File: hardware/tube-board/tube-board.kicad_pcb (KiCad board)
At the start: 2 copper layers, 182 x 26 mm, 18 parts, among them J1 CONN_01X10, J2 CONN_01X10, U1 HV5522PG, U2 HV5522PG

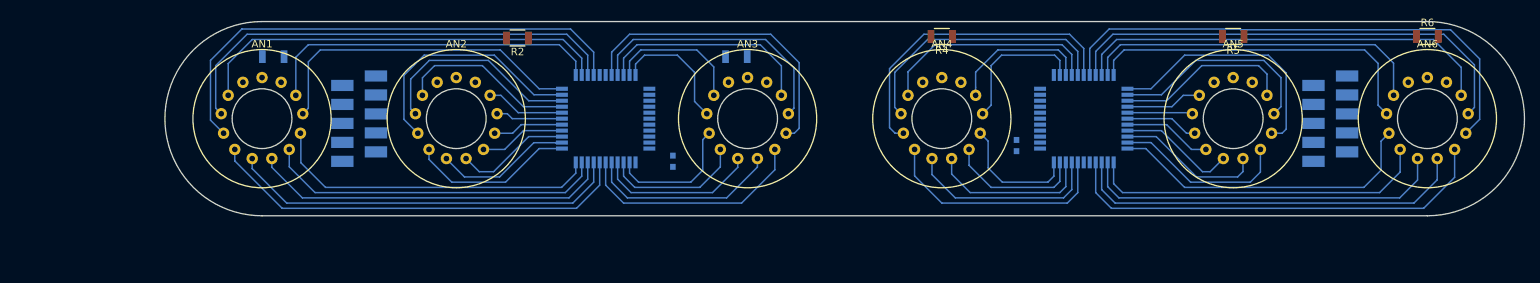
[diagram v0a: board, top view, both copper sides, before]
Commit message: Working on tube board layout
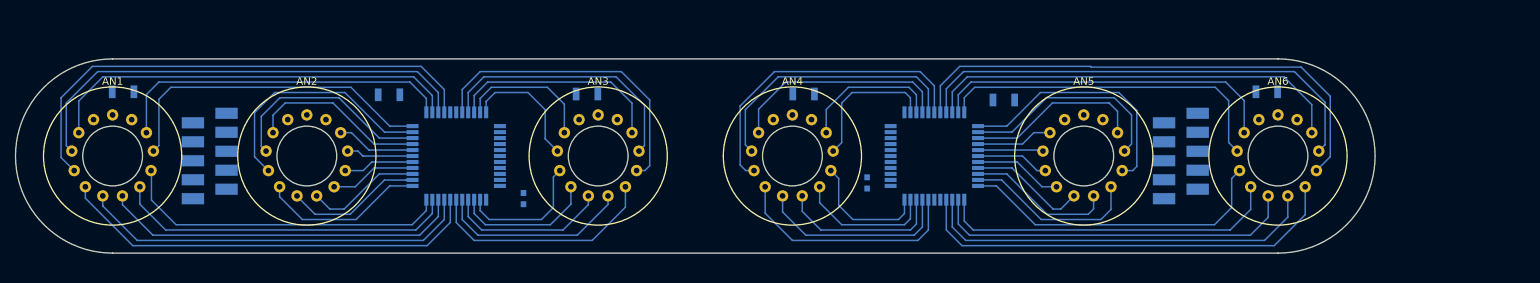
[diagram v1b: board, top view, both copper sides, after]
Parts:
- R2, R4, R5, R6: moved to B.Cu
- moved R5 31.9 mm to (181.3, 97.5), turned to 0 degrees
- moved R6 22.7 mm to (216.5, 96.4)
- moved R1 20.6 mm to (63.4, 96.4)
- moved AN1 20.6 mm to (62.0, 105.0)
- moved AN2 20.6 mm to (88.0, 105.0)
- moved AN3 20.6 mm to (127.0, 105.0)
- moved AN4 20.6 mm to (153.0, 105.0)
- moved AN5 20.6 mm to (192.0, 105.0)
- moved AN6 20.6 mm to (218.0, 105.0)
- moved C1 20.6 mm to (117.0, 110.7)
- moved C2 20.6 mm to (163.0, 108.6)
- moved J1 20.6 mm to (75.0, 105.0)
- moved J2 20.6 mm to (205.0, 105.0)
- moved R3 20.6 mm to (125.5, 96.7)
- moved U1 20.6 mm to (108.0, 105.0)
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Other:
- net class Default: trace_width 0.25 -> 0.2; via_dia 0.6 -> 0.5; via_drill 0.4 -> 0.34
- rule pad_to_mask_clearance: 0.2 -> 0.05

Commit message: Working on tube board layout
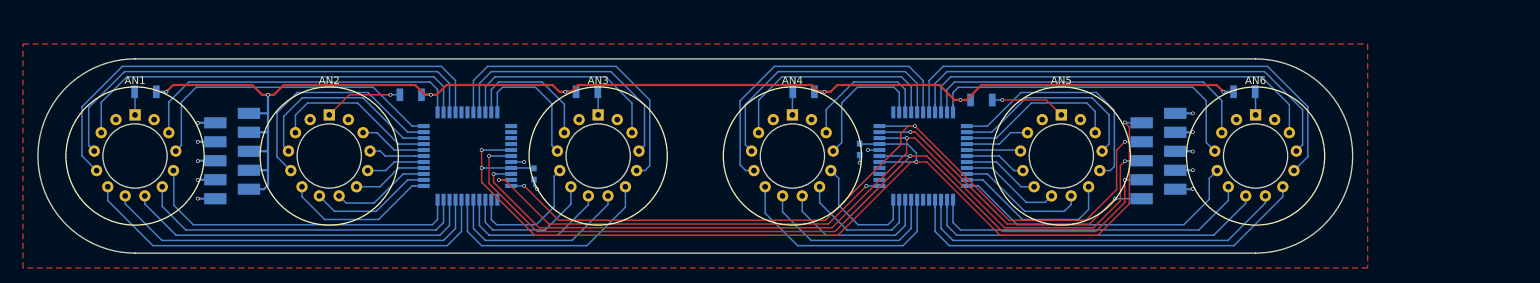
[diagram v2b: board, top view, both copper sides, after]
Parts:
- moved C2 4.61 mm to (162.0, 104.1), turned to 270 degrees
- moved C1 3.58 mm to (118.4, 107.4)
- moved R1 3.00 mm to (66.4, 96.4)
- moved AN1 3.00 mm to (65.0, 105.0)
- moved AN2 3.00 mm to (91.0, 105.0)
- moved AN5 3.00 mm to (189.0, 105.0)
- moved AN6 3.00 mm to (215.0, 105.0)
- moved J1 3.00 mm to (78.0, 105.0)
- moved J2 3.00 mm to (202.0, 105.0)
- moved R5 3.00 mm to (178.3, 97.5)
- moved R6 3.00 mm to (213.5, 96.4)
- moved R2 2.90 mm to (101.9, 96.8)
- moved U1 1.50 mm to (109.5, 105.0)
- moved U2 1.50 mm to (170.5, 105.0)
- moved R3 0.30 mm to (125.5, 96.4)
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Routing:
- net HT: track 0.00 -> 180.8 mm, vias 0 -> 7
- net +12V: track 0.00 -> 142.5 mm, vias 0 -> 4
- net /LE: track 0.00 -> 114.0 mm, vias 0 -> 3
- net /CLK: track 0.00 -> 113.8 mm, vias 0 -> 3
- net /BL: track 0.00 -> 109.8 mm, vias 0 -> 3
- net Net-(U1-Pad32): track 0.00 -> 57.2 mm, vias 0 -> 2
- net /DATA_IN: track 0.00 -> 41.6 mm, vias 0 -> 2
- net GND: track 0.00 -> 29.4 mm, vias 0 -> 14
- net Net-(AN2-Pad1): track 0.00 -> 10.6 mm, vias 0 -> 1
- net Net-(AN5-Pad1): track 0.00 -> 10.1 mm, vias 0 -> 1
- net Net-(AN6-Pad1): track 0.00 -> 3.12 mm
- net Net-(AN4-Pad1): track 0.00 -> 3.12 mm
- net Net-(AN3-Pad1): track 0.00 -> 3.12 mm
- net Net-(AN1-Pad1): track 0.00 -> 3.12 mm
- net /HV57: track 58.4 -> 55.6 mm
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- added copper zone on F.Cu, net GND
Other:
- board size 182 x 26 mm -> 176 x 26 mm

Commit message: Working on tube board layout
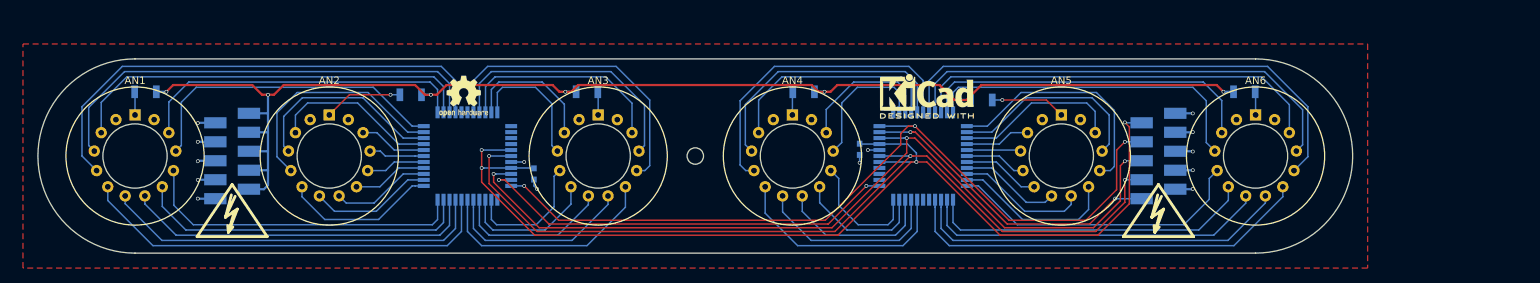
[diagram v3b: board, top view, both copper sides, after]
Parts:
- added REF**: Symbol_HighVoltage_Type2_CopperTop_VerySmall, radio-clock:Symbol_HighVoltage_Type2_SilkscreenTop_VerySmall, F.Cu at (202.0, 113.0)
- added REF**: MountingHole_2.2mm_M2, Mounting_Holes:MountingHole_2.2mm_M2, B.Cu at (140.0, 105.0)
- added REF**: Symbol_HighVoltage_Type2_CopperTop_VerySmall, radio-clock:Symbol_HighVoltage_Type2_SilkscreenTop_VerySmall, F.Cu at (78.0, 113.0)
- added REF***: OSHW-Logo2_7.3x6mm_SilkScreen, Symbols:OSHW-Logo2_7.3x6mm_SilkScreen, F.Cu at (109.0, 97.0)
- added REF***: KiCad-Logo2_6mm_SilkScreen, Symbols:KiCad-Logo2_6mm_SilkScreen, F.Cu at (171.0, 97.0)

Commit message: Working on main board schematic
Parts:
- removed the REF** at (202.0, 113.0)
- moved REF*** 62.8 mm to (170.0, 112.0)
- moved REF** 31.1 mm to (109.0, 111.0)
- moved REF*** 1.00 mm to (171.0, 98.0)
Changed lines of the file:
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@@
     (links 103)
     (no_connects 0)
-    (area 51.924999 91.924999 228.075001 118.075001)
+    (area 50 90 230.000001 120.000001)
     (thickness 1.6)
     (drawings 10)
     (tracks 540)
     (zones 0)
-    (modules 23)
+    (modules 22)
     (nets 100)
   )
@@
     (add_net /HV9)
   )
-  (module radio-clock:Symbol_HighVoltage_Type2_SilkscreenTop_VerySmall (layer F.Cu)
-    (at 202 113)
-    (descr "Symbol, High Voltage, Type 2, Copper Top, Very Small,")
-    (tags "Symbol, High Voltage, Type 2, Copper Top, Very Small,")
-    (fp_text reference REF** (at -0.127 -5.715) (layer F.SilkS) hide
-      (effects (font (size 1 1) (thickness 0.15)))
-    )
-    (fp_text value Symbol_HighVoltage_Type2_CopperTop_VerySmall (at -0.381 4.572) (layer F.Fab)
-      (effects (font (size 1 1) (thickness 0.15)))
-    )
-    (fp_line (start -0.49784 2.19964) (end 0.70104 -0.89916) (layer F.SilkS) (width 0.381))
-    (fp_line (start 0.70104 -0.89916) (end 0.1016 -0.50038) (layer F.SilkS) (width 0.381))
-    (fp_line (start -0.89916 0.20066) (end 0.40132 -2.60096) (layer F.SilkS) (width 0.381))
-    (fp_line (start -0.49784 2.19964) (end 0.1016 1.50114) (layer F.SilkS) (width 0.381))
-    (fp_line (start -0.09906 -2.79908) (end -0.89916 0.20066) (layer F.SilkS) (width 0.381))
-    (fp_line (start -0.89916 0.20066) (end 0.29972 -0.59944) (layer F.SilkS) (width 0.381))
-    (fp_line (start 0.29972 -0.59944) (end -0.49784 2.19964) (layer F.SilkS) (width 0.381))
-    (fp_line (start -0.49784 2.19964) (end -0.59944 1.30048) (layer F.SilkS) (width 0.381))
-    (fp_line (start 0 -4.191) (end 4.699 2.794) (layer F.SilkS) (width 0.381))
-    (fp_line (start 4.699 2.794) (end -4.699 2.794) (layer F.SilkS) (width 0.381))
-    (fp_line (start -4.699 2.794) (end 0 -4.191) (layer F.SilkS) (width 0.381))
-  )
   (module Capacitors_SMD:C_0603 (layer B.Cu)
     (at 118.4 107.4 270)
@@
   )
   (module Symbols:OSHW-Logo2_7.3x6mm_SilkScreen (layer F.Cu)
-    (at 109 97)
+    (at 170 112)
     (descr "Open Source Hardware Symbol")
     (tags "Logo Symbol OSHW")
@@
   )
   (module Symbols:KiCad-Logo2_6mm_SilkScreen (layer F.Cu)
-    (at 171 97)
+    (at 171 98)
     (descr "KiCad Logo")
     (tags "Logo KiCad")
@@
   )
   (module radio-clock:Symbol_HighVoltage_Type2_SilkscreenTop_VerySmall (layer F.Cu)
-    (at 78 113)
+    (at 109 111)
     (descr "Symbol, High Voltage, Type 2, Copper Top, Very Small,")
     (tags "Symbol, High Voltage, Type 2, Copper Top, Very Small,")

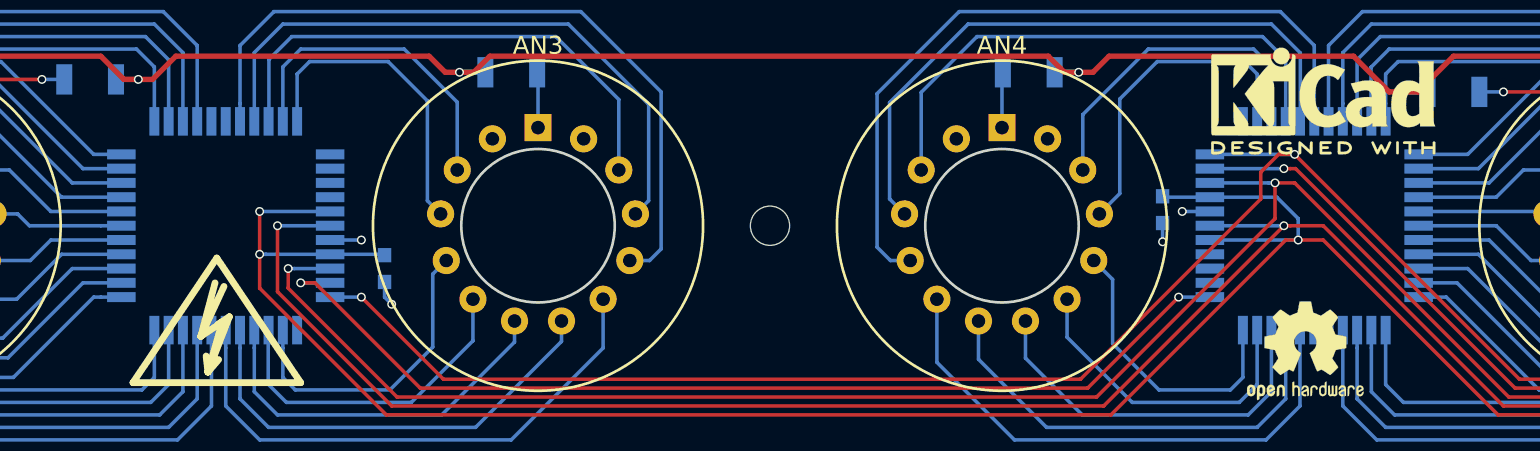
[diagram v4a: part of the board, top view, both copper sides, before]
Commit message: Modified HV5522 footprint to have oval pads
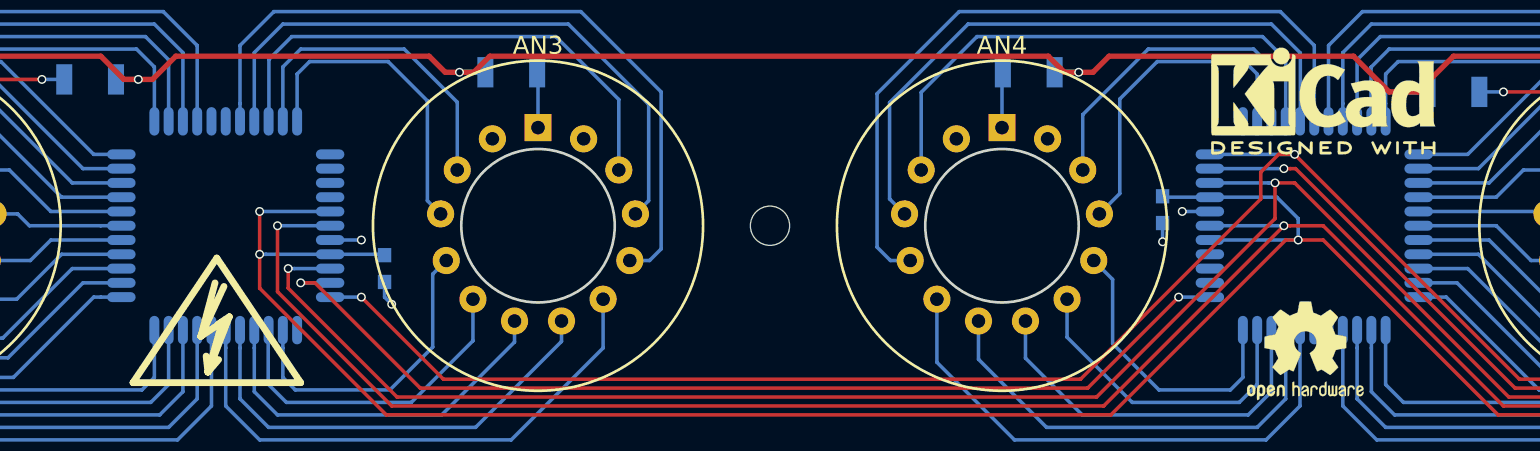
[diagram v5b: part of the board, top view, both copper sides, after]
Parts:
- U1, U2: footprint Housings_QFP:LQFP-44_10x10mm_Pitch0.8mm -> radio-clock:LQFP-44_10x10mm_Pitch0.8mm_Rounded

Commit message: Finished tube board
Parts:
- removed the REF*** at (170.0, 112.0)
- added REF**: Symbol_HighVoltage_Type2_CopperTop_VerySmall, radio-clock:Symbol_HighVoltage_Type2_SilkscreenTop_VerySmall, F.Cu at (202.0, 113.0)
- added REF***: OSHW-Logo2_9.8x8mm_SilkScreen, Symbols:OSHW-Logo2_9.8x8mm_SilkScreen, F.Cu at (170.0, 97.5)
- C1, C2: footprint Capacitors_SMD:C_0603 -> Capacitors_SMD:C_0805
- moved REF*** 62.0 mm to (109.0, 97.5)
- moved REF** 31.1 mm to (78.0, 113.0)
- moved C2 1.71 mm to (161.8, 102.4), turned to 90 degrees
- moved C1 0.22 mm to (118.5, 107.6)
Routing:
- net HT: track 180.8 -> 182.7 mm
- net /HV57: track 55.6 -> 56.2 mm
- net /HV6: track 56.7 -> 57.3 mm
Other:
- board text added: "FRONT"

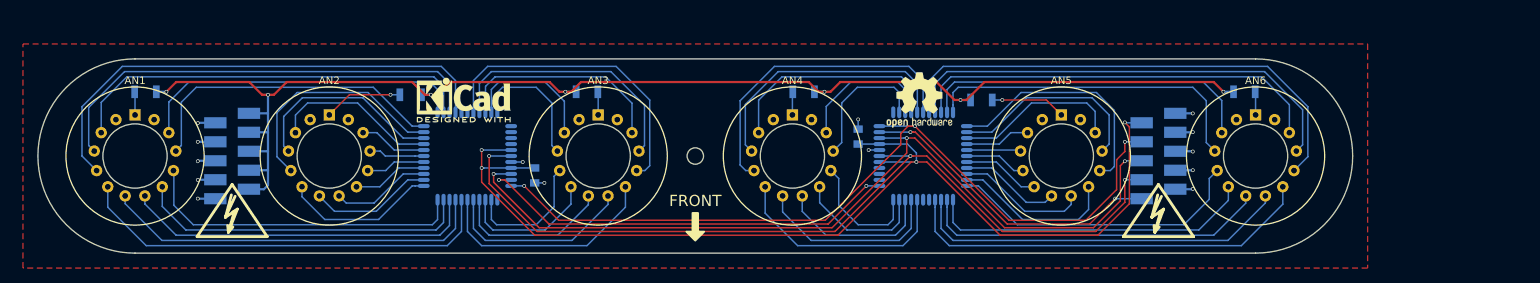
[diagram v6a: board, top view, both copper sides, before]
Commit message: Fixed HV5522 footprint on tube board.  Increased size of IN-14 through holes.  Fixed footprint for MOSFET in HV boost circuit.  Fixed hole size for battery holder footprint.
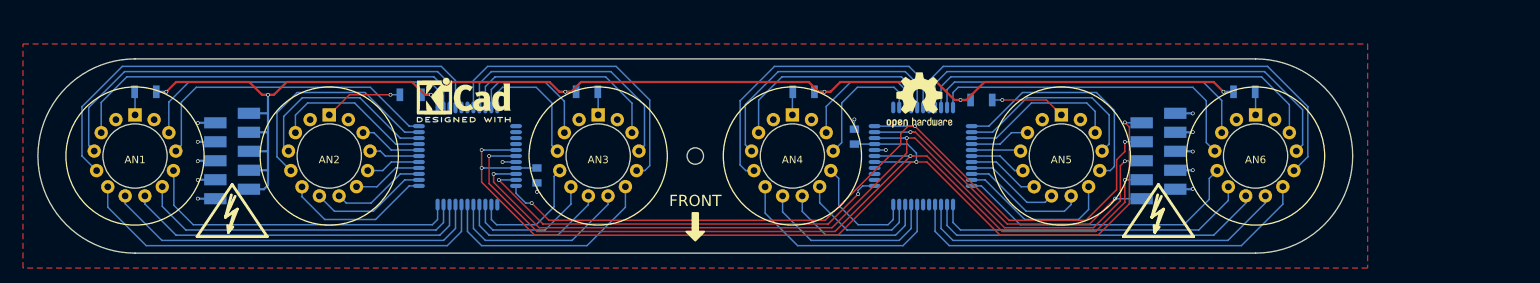
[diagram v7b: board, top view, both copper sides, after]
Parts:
- moved C2 0.50 mm to (161.3, 102.4)
- moved C1 0.30 mm to (118.8, 107.6)
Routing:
- net +12V: track 142.7 -> 144.8 mm
- net /CLK: track 113.8 -> 115.1 mm
- net /LE: track 114.0 -> 115.3 mm
- net /HV2: track 18.7 -> 18.0 mm
- net /HV36: track 35.9 -> 35.3 mm
- net /HV41: track 45.6 -> 44.9 mm
- net /DATA_IN: track 41.6 -> 42.3 mm
- net /HV54: track 43.8 -> 43.1 mm
- net /HV21: track 42.3 -> 41.6 mm
- net /HV14: track 10.0 -> 9.40 mm
- net /HV9: track 45.1 -> 44.4 mm
- net /HV8: track 47.6 -> 46.9 mm
- net /HV7: track 51.8 -> 51.2 mm
- net /HV64: track 16.4 -> 15.8 mm
- net /HV63: track 17.8 -> 17.1 mm
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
